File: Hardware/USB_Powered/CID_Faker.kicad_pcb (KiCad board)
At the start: 2 copper layers, 26.5 x 39.8 mm, 4 parts, among them J1 PWR, J2 CAN, U1 ProMicro, U2 LF80_TO220

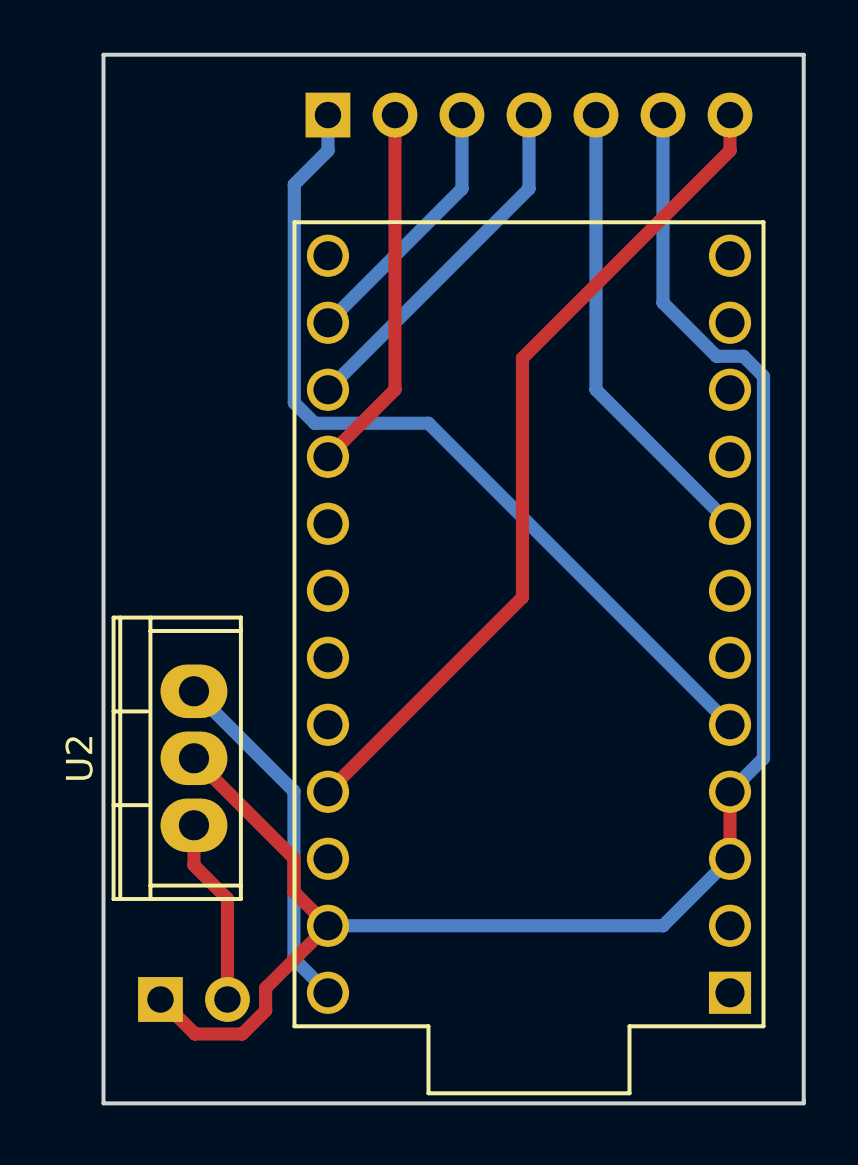
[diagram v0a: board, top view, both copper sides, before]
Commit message: Updated USB powered version schematics
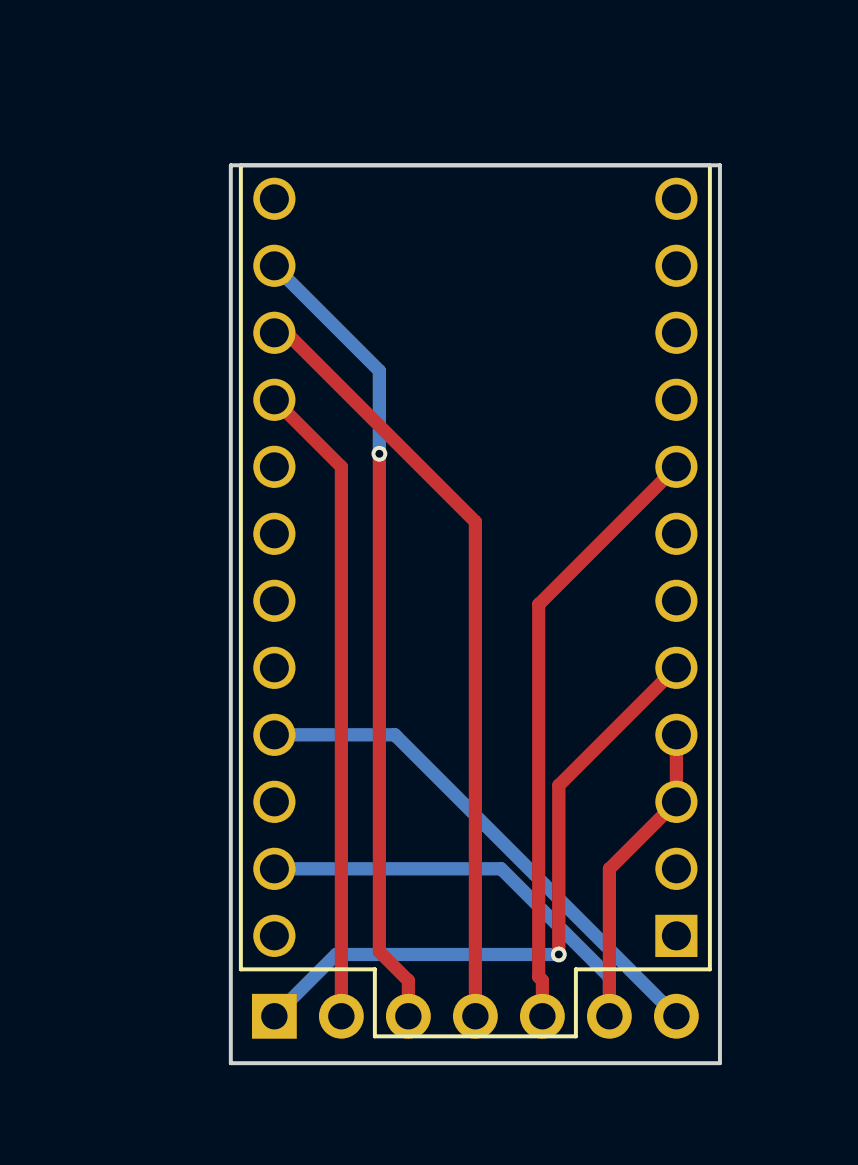
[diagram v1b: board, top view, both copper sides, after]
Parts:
- removed J1: PWR, Pin_Headers:Pin_Header_Angled_1x02_Pitch2.54mm
- removed U2: LF80_TO220, Power_Integrations:TO-220
- moved J2 34.2 mm to (127.0, 122.3)
- moved U1 2.96 mm to (134.6, 105.3)
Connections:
- U1 pad 24: RAW -> (no net)
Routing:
- net GND: track 64.7 -> 27.6 mm
- net MOSI: track 9.98 -> 30.6 mm, vias 0 -> 1
- net MISO: track 13.6 -> 29.3 mm
- net RAW: track 13.5 -> 0.00 mm
- net VCC: track 32.0 -> 19.7 mm
- net SCK: track 14.0 -> 24.4 mm
- net INT: track 33.0 -> 24.5 mm, vias 0 -> 1
- net VIN: track 7.13 -> 0.00 mm
- net CS: track 17.6 -> 23.0 mm
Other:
- board size 26.5 x 39.8 mm -> 18.5 x 34 mm

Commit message: upgraded to kicad 5 updated schematics and PCB
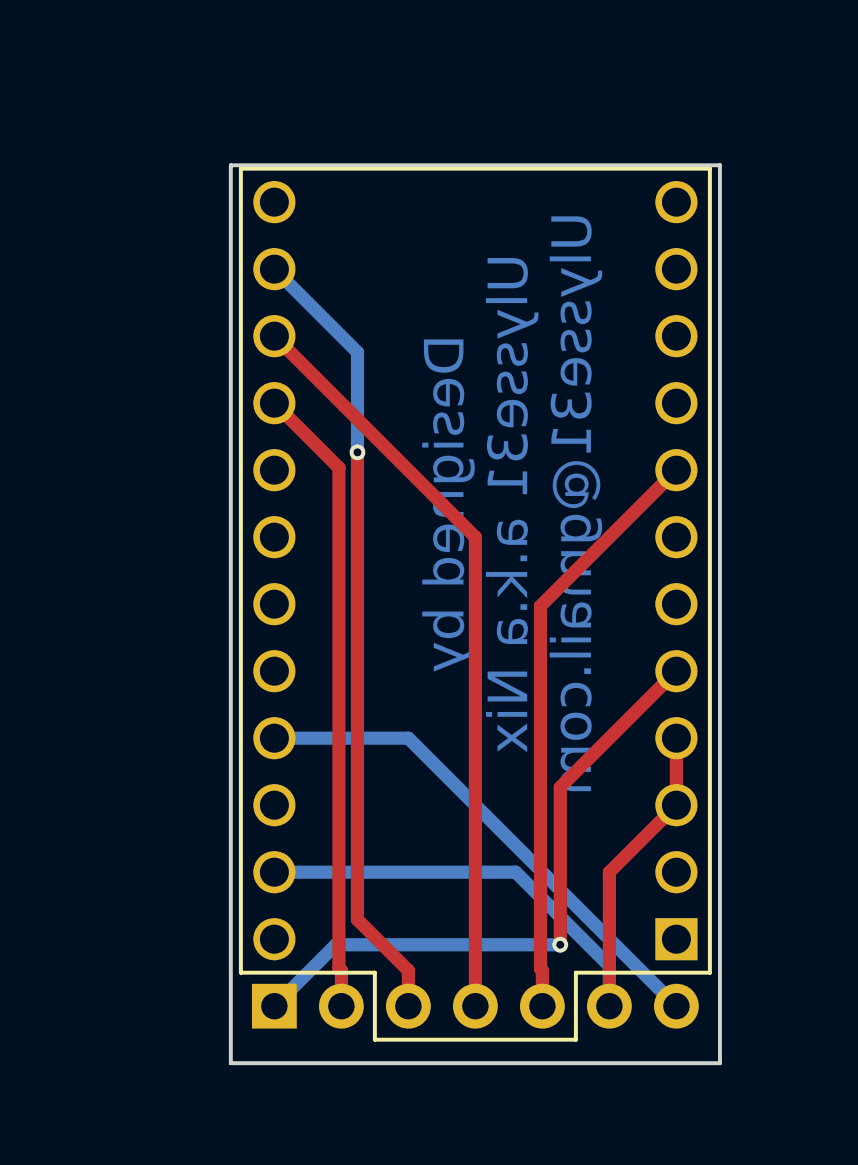
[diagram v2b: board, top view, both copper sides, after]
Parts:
- removed J2: CAN, Socket_Strips:Socket_Strip_Straight_1x07_Pitch2.54mm
- added J1: CAN1, Connector_PinSocket_2.54mm:PinSocket_1x07_P2.54mm_Vertical, B.Cu at (127.0, 121.9)
- moved U1 0.13 mm to (134.6, 105.4)
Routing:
- net MISO: track 29.3 -> 28.6 mm
- net GND: track 27.6 -> 26.9 mm
- net CS: track 23.0 -> 22.5 mm
- net MOSI: track 30.6 -> 30.0 mm
- net SCK: track 24.4 -> 23.9 mm
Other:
- board text added: "Designed by Ulysse31 a.k.a Nix Ulysse31@gmail.com"

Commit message: Updated schema : longer but smaller ^^' (possibility to solder arduino and mcp module directly without header connectors)
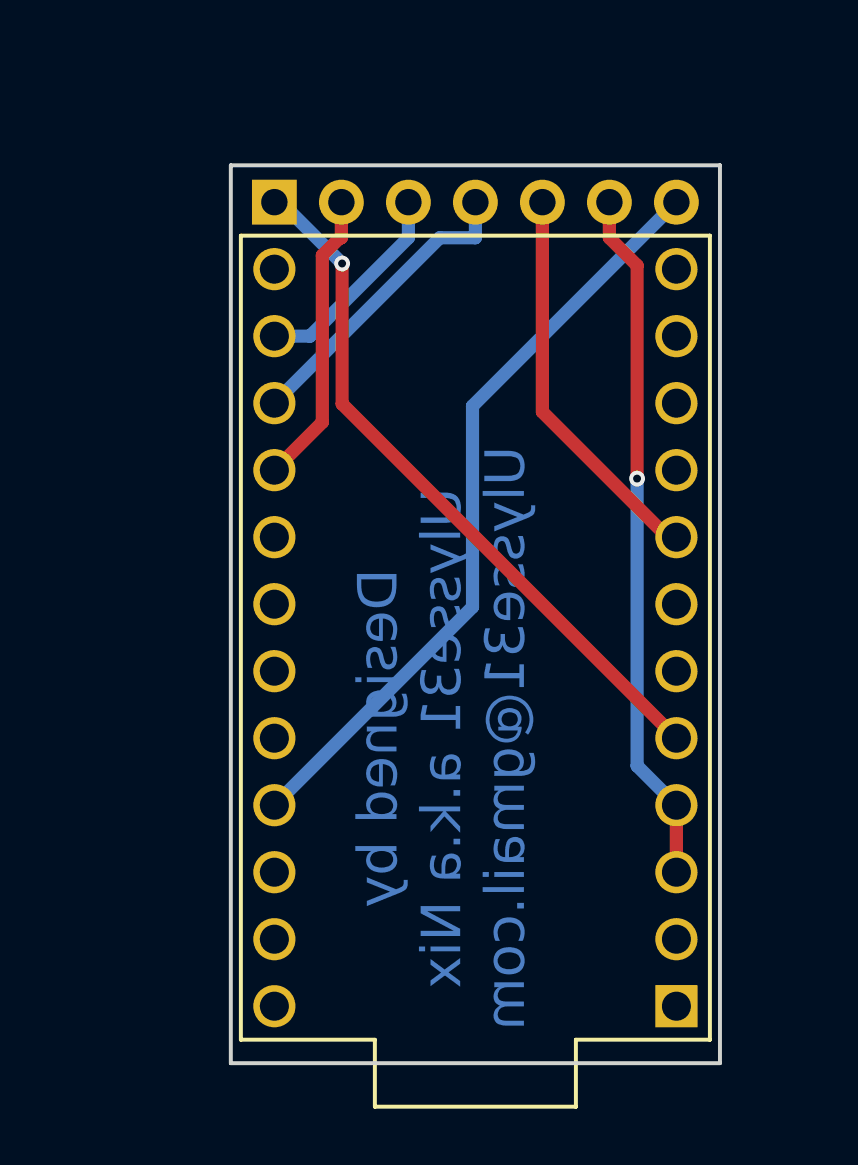
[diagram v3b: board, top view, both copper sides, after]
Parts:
- moved J1 30.5 mm to (127.0, 91.4)
- moved U1 2.54 mm to (134.6, 108.0)
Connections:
- U1 pad 23: GND -> (no net)
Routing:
- net MOSI: track 30.0 -> 7.98 mm, vias 1 -> 0
- net MISO: track 28.6 -> 11.6 mm
- net SCK: track 23.9 -> 11.2 mm
- net VCC: track 19.4 -> 29.2 mm
- net CS: track 22.5 -> 15.0 mm
- net INT: track 24.0 -> 26.8 mm
- net GND: track 26.9 -> 26.5 mm, vias 0 -> 1
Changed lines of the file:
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@@
     (thickness 1.6)
     (drawings 5)
-    (tracks 30)
+    (tracks 29)
     (zones 0)
     (modules 2)
@@
   )
   (module Connector_PinSocket_2.54mm:PinSocket_1x07_P2.54mm_Vertical (layer B.Cu)
-    (at 127 121.92 270)
+    (at 127 91.44 270)
     (descr "Through hole straight socket strip, 1x07, 2.54mm pitch, single row (from Kicad 4.0.7), script generated")
     (tags "Through hole socket strip THT 1x07 2.54mm single row")
@@
   )
   (module promicro:ProMicro (layer F.Cu)
-    (at 134.62 105.41 90)
+    (at 134.62 107.95 90)
     (descr "Pro Micro footprint")
     (tags "promicro ProMicro")
@@
       (net 7 VCC))
     (pad 22 thru_hole circle (at -8.89 -7.62 90) (size 1.6 1.6) (drill 1.1) (layers *.Cu *.Mask F.SilkS))
-    (pad 23 thru_hole circle (at -11.43 -7.62 90) (size 1.6 1.6) (drill 1.1) (layers *.Cu *.Mask F.SilkS)
-      (net 1 GND))
+    (pad 23 thru_hole circle (at -11.43 -7.62 90) (size 1.6 1.6) (drill 1.1) (layers *.Cu *.Mask F.SilkS))
     (pad 24 thru_hole circle (at -13.97 -7.62 90) (size 1.6 1.6) (drill 1.1) (layers *.Cu *.Mask F.SilkS))
   )
-  (gr_text "Designed by\nUlysse31 a.k.a Nix\nUlysse31@gmail.com\n" (at 135.89 102.87 90) (layer B.Cu)
+  (gr_text "Designed by\nUlysse31 a.k.a Nix\nUlysse31@gmail.com\n" (at 133.35 111.76 90) (layer B.Cu)
     (effects (font (size 1.5 1.5) (thickness 0.3)) (justify mirror))
   )
@@
   (gr_line (start 125.349 124.079) (end 125.349 90.043) (angle 90) (layer Edge.Cuts) (width 0.15))
   (gr_line (start 143.891 124.079) (end 125.349 124.079) (angle 90) (layer Edge.Cuts) (width 0.15))
-  (segment (start 139.7 120.57) (end 139.7 120.3918) (width 0.5) (layer B.Cu) (net 1))
-  (segment (start 139.7 120.3918) (end 136.1482 116.84) (width 0.5) (layer B.Cu) (net 1))
-  (segment (start 136.1482 116.84) (end 127 116.84) (width 0.5) (layer B.Cu) (net 1))
-  (segment (start 142.24 114.3) (end 139.7 116.84) (width 0.5) (layer F.Cu) (net 1))
-  (segment (start 139.7 116.84) (end 139.7 121.92) (width 0.5) (layer F.Cu) (net 1))
-  (segment (start 142.24 111.76) (end 142.24 114.3) (width 0.5) (layer F.Cu) (net 1))
-  (segment (start 139.7 121.92) (end 139.7 120.57) (width 0.5) (layer B.Cu) (net 1))
-  (segment (start 137.8372 119.5902) (end 129.3298 119.5902) (width 0.5) (layer B.Cu) (net 2))
-  (segment (start 129.3298 119.5902) (end 127 121.92) (width 0.5) (layer B.Cu) (net 2))
-  (segment (start 142.24 109.22) (end 137.8372 113.6228) (width 0.5) (layer F.Cu) (net 2))
-  (segment (start 137.8372 113.6228) (end 137.8372 119.5902) (width 0.5) (layer F.Cu) (net 2))
-  (via (at 137.8372 119.5902) (size 0.6) (layers F.Cu B.Cu) (net 2))
-  (segment (start 127 99.06) (end 129.4467 101.5067) (width 0.5) (layer F.Cu) (net 3))
-  (segment (start 129.4467 101.5067) (end 129.4467 120.4767) (width 0.5) (layer F.Cu) (net 3))
-  (segment (start 129.4467 120.4767) (end 129.54 120.57) (width 0.5) (layer F.Cu) (net 3))
-  (segment (start 129.54 121.92) (end 129.54 120.57) (width 0.5) (layer F.Cu) (net 3))
-  (segment (start 132.08 120.57) (end 130.1504 118.6404) (width 0.5) (layer F.Cu) (net 4))
-  (segment (start 130.1504 118.6404) (end 130.1504 100.9245) (width 0.5) (layer F.Cu) (net 4))
-  (segment (start 127 93.98) (end 130.1504 97.1304) (width 0.5) (layer B.Cu) (net 4))
-  (segment (start 130.1504 97.1304) (end 130.1504 100.9245) (width 0.5) (layer B.Cu) (net 4))
-  (segment (start 132.08 121.92) (end 132.08 120.57) (width 0.5) (layer F.Cu) (net 4))
-  (via (at 130.1504 100.9245) (size 0.6) (layers F.Cu B.Cu) (net 4))
-  (segment (start 127 96.52) (end 134.62 104.14) (width 0.5) (layer F.Cu) (net 5))
-  (segment (start 134.62 104.14) (end 134.62 121.92) (width 0.5) (layer F.Cu) (net 5))
-  (segment (start 142.24 101.6) (end 137.0869 106.7531) (width 0.5) (layer F.Cu) (net 6))
-  (segment (start 137.0869 106.7531) (end 137.0869 120.4969) (width 0.5) (layer F.Cu) (net 6))
-  (segment (start 137.0869 120.4969) (end 137.16 120.57) (width 0.5) (layer F.Cu) (net 6))
-  (segment (start 137.16 121.92) (end 137.16 120.57) (width 0.5) (layer F.Cu) (net 6))
-  (segment (start 127 111.76) (end 132.08 111.76) (width 0.5) (layer B.Cu) (net 7))
-  (segment (start 132.08 111.76) (end 142.24 121.92) (width 0.5) (layer B.Cu) (net 7))
+  (segment (start 139.7 91.44) (end 139.7 92.79) (width 0.5) (layer F.Cu) (net 1))
+  (segment (start 140.7495 101.9195) (end 140.7495 93.8395) (width 0.5) (layer F.Cu) (net 1))
+  (segment (start 140.7495 93.8395) (end 139.7 92.79) (width 0.5) (layer F.Cu) (net 1))
+  (segment (start 142.24 114.3) (end 140.7495 112.8095) (width 0.5) (layer B.Cu) (net 1))
+  (segment (start 140.7495 112.8095) (end 140.7495 101.9195) (width 0.5) (layer B.Cu) (net 1))
+  (segment (start 142.24 114.3) (end 142.24 116.84) (width 0.5) (layer F.Cu) (net 1))
+  (via (at 140.7495 101.9195) (size 0.6) (layers F.Cu B.Cu) (net 1))
+  (segment (start 127 91.44) (end 127.2429 91.44) (width 0.5) (layer B.Cu) (net 2))
+  (segment (start 127.2429 91.44) (end 129.5683 93.7654) (width 0.5) (layer B.Cu) (net 2))
+  (segment (start 142.24 111.76) (end 129.5683 99.0883) (width 0.5) (layer F.Cu) (net 2))
+  (segment (start 129.5683 99.0883) (end 129.5683 93.7654) (width 0.5) (layer F.Cu) (net 2))
+  (via (at 129.5683 93.7654) (size 0.6) (layers F.Cu B.Cu) (net 2))
+  (segment (start 129.54 92.79) (end 129.4826 92.79) (width 0.5) (layer F.Cu) (net 3))
+  (segment (start 129.4826 92.79) (end 128.818 93.4546) (width 0.5) (layer F.Cu) (net 3))
+  (segment (start 128.818 93.4546) (end 128.818 99.782) (width 0.5) (layer F.Cu) (net 3))
+  (segment (start 128.818 99.782) (end 127 101.6) (width 0.5) (layer F.Cu) (net 3))
+  (segment (start 129.54 91.44) (end 129.54 92.79) (width 0.5) (layer F.Cu) (net 3))
+  (segment (start 132.08 91.44) (end 132.08 92.79) (width 0.5) (layer B.Cu) (net 4))
+  (segment (start 127 96.52) (end 128.35 96.52) (width 0.5) (layer B.Cu) (net 4))
+  (segment (start 128.35 96.52) (end 132.08 92.79) (width 0.5) (layer B.Cu) (net 4))
+  (segment (start 134.62 91.44) (end 134.62 92.79) (width 0.5) (layer B.Cu) (net 5))
+  (segment (start 127 99.06) (end 133.27 92.79) (width 0.5) (layer B.Cu) (net 5))
+  (segment (start 133.27 92.79) (end 134.62 92.79) (width 0.5) (layer B.Cu) (net 5))
+  (segment (start 137.16 91.44) (end 137.16 99.3911) (width 0.5) (layer F.Cu) (net 6))
+  (segment (start 137.16 99.3911) (end 141.9089 104.14) (width 0.5) (layer F.Cu) (net 6))
+  (segment (start 141.9089 104.14) (end 142.24 104.14) (width 0.5) (layer F.Cu) (net 6))
+  (segment (start 127 114.3) (end 134.511 106.789) (width 0.5) (layer B.Cu) (net 7))
+  (segment (start 134.511 106.789) (end 134.511 99.169) (width 0.5) (layer B.Cu) (net 7))
+  (segment (start 134.511 99.169) (end 142.24 91.44) (width 0.5) (layer B.Cu) (net 7))
 )
